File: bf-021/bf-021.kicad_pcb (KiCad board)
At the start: 2 copper layers, 50 x 50 mm, 9 parts, among them J1 M-BUS

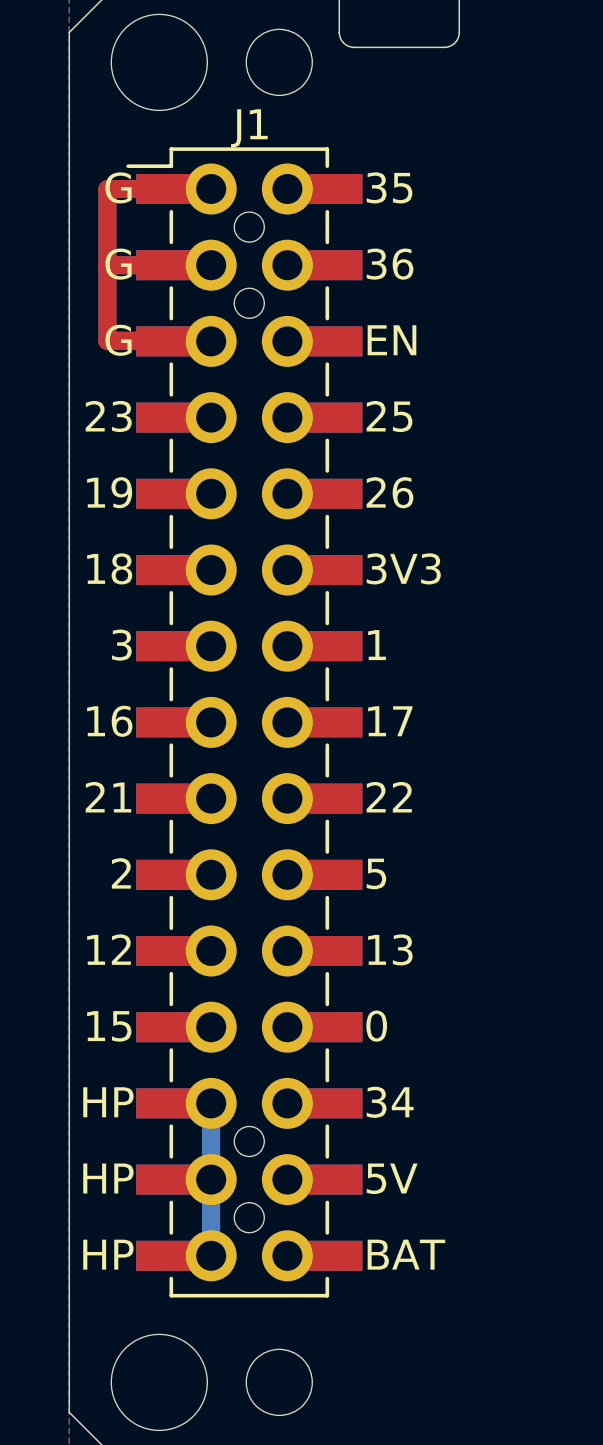
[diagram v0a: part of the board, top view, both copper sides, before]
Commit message: refine drawing representations
Correcting mistakes in chamfer dimension description values
Change grid origin to center
Added GPIO reference
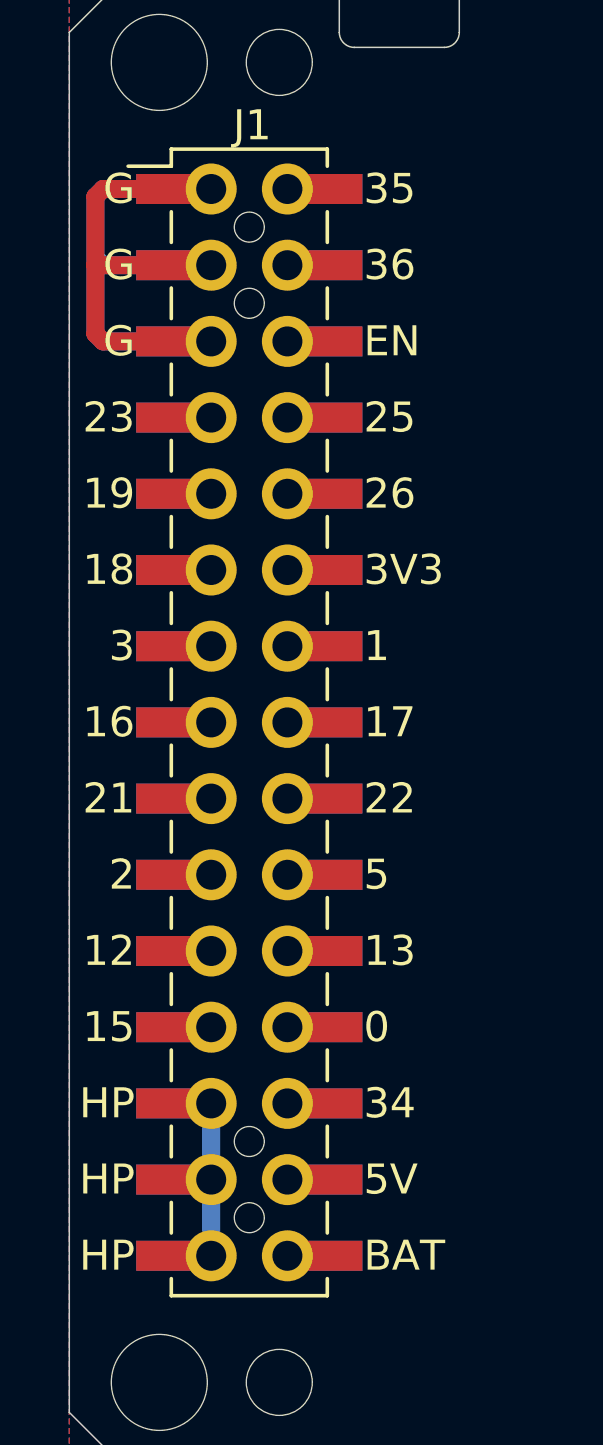
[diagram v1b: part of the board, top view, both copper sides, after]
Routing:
- net GND: track 30.9 -> 32.8 mm
